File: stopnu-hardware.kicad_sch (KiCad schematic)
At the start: 5 parts, among them CN1 SM04B-SRSS-TB (LF)(SN)

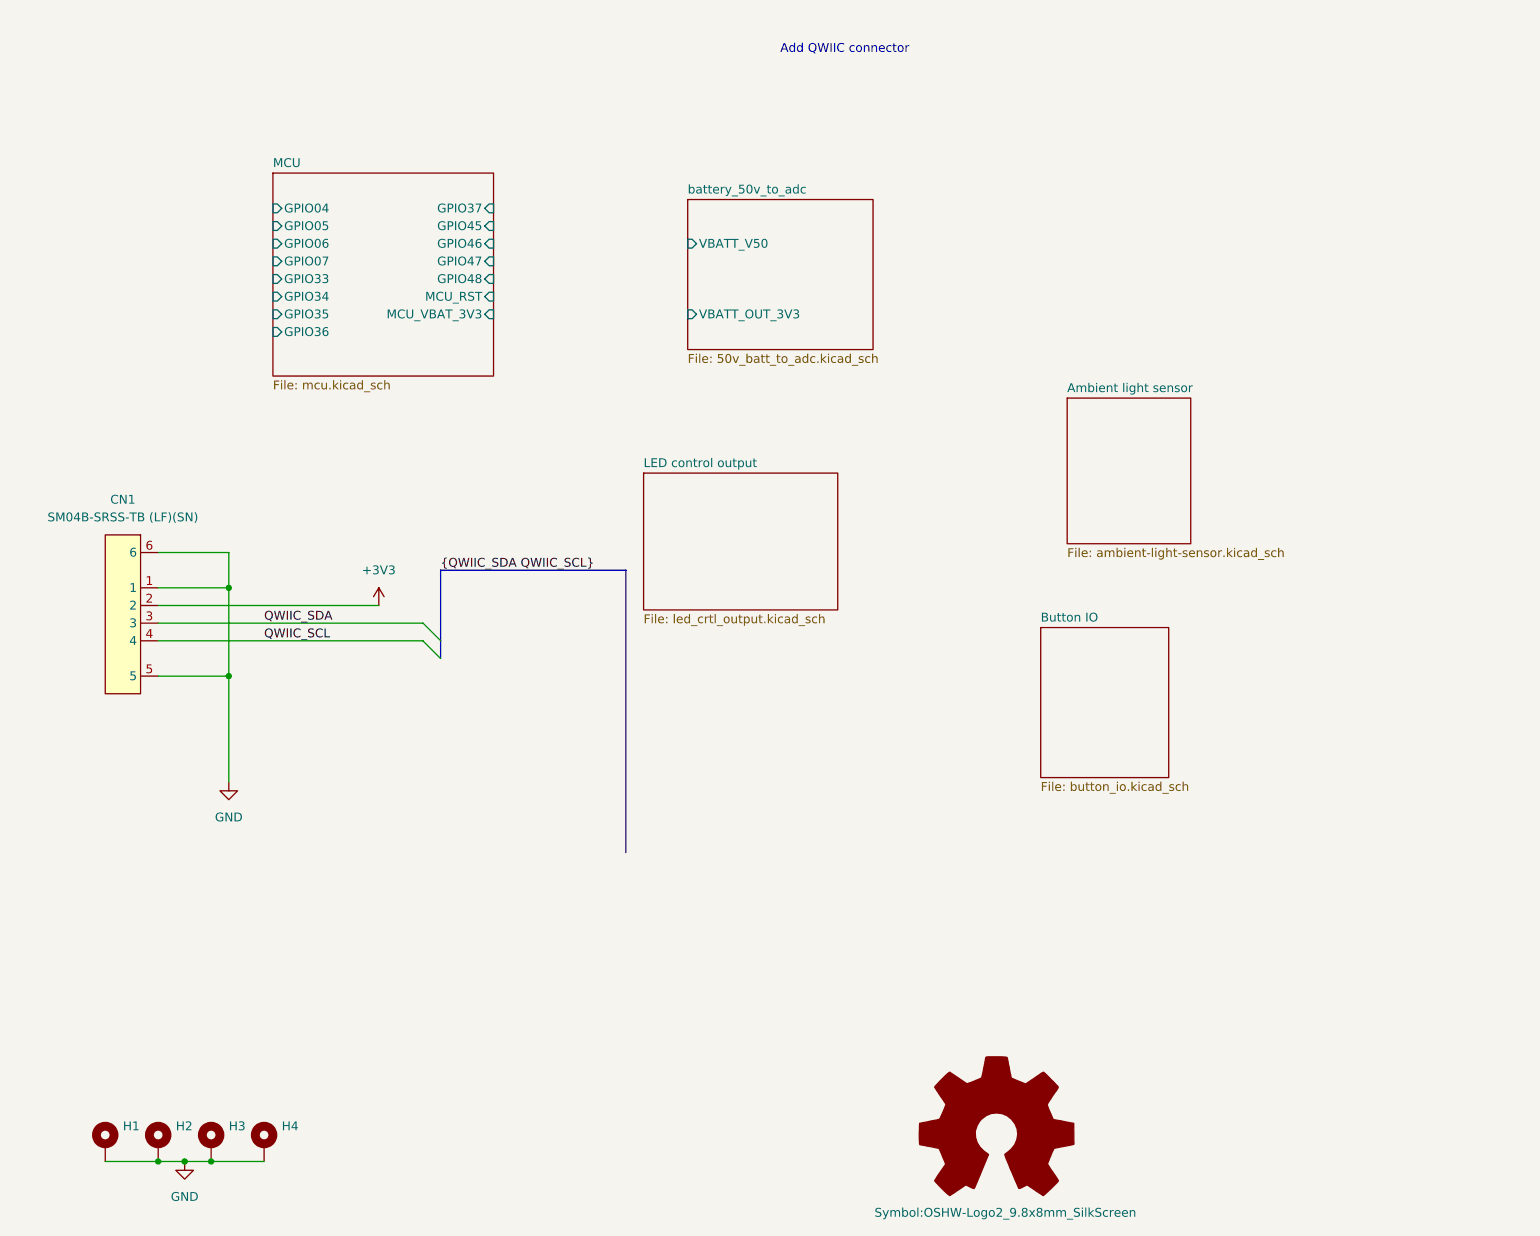
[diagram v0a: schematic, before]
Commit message: Place opto couplers and some connectors.
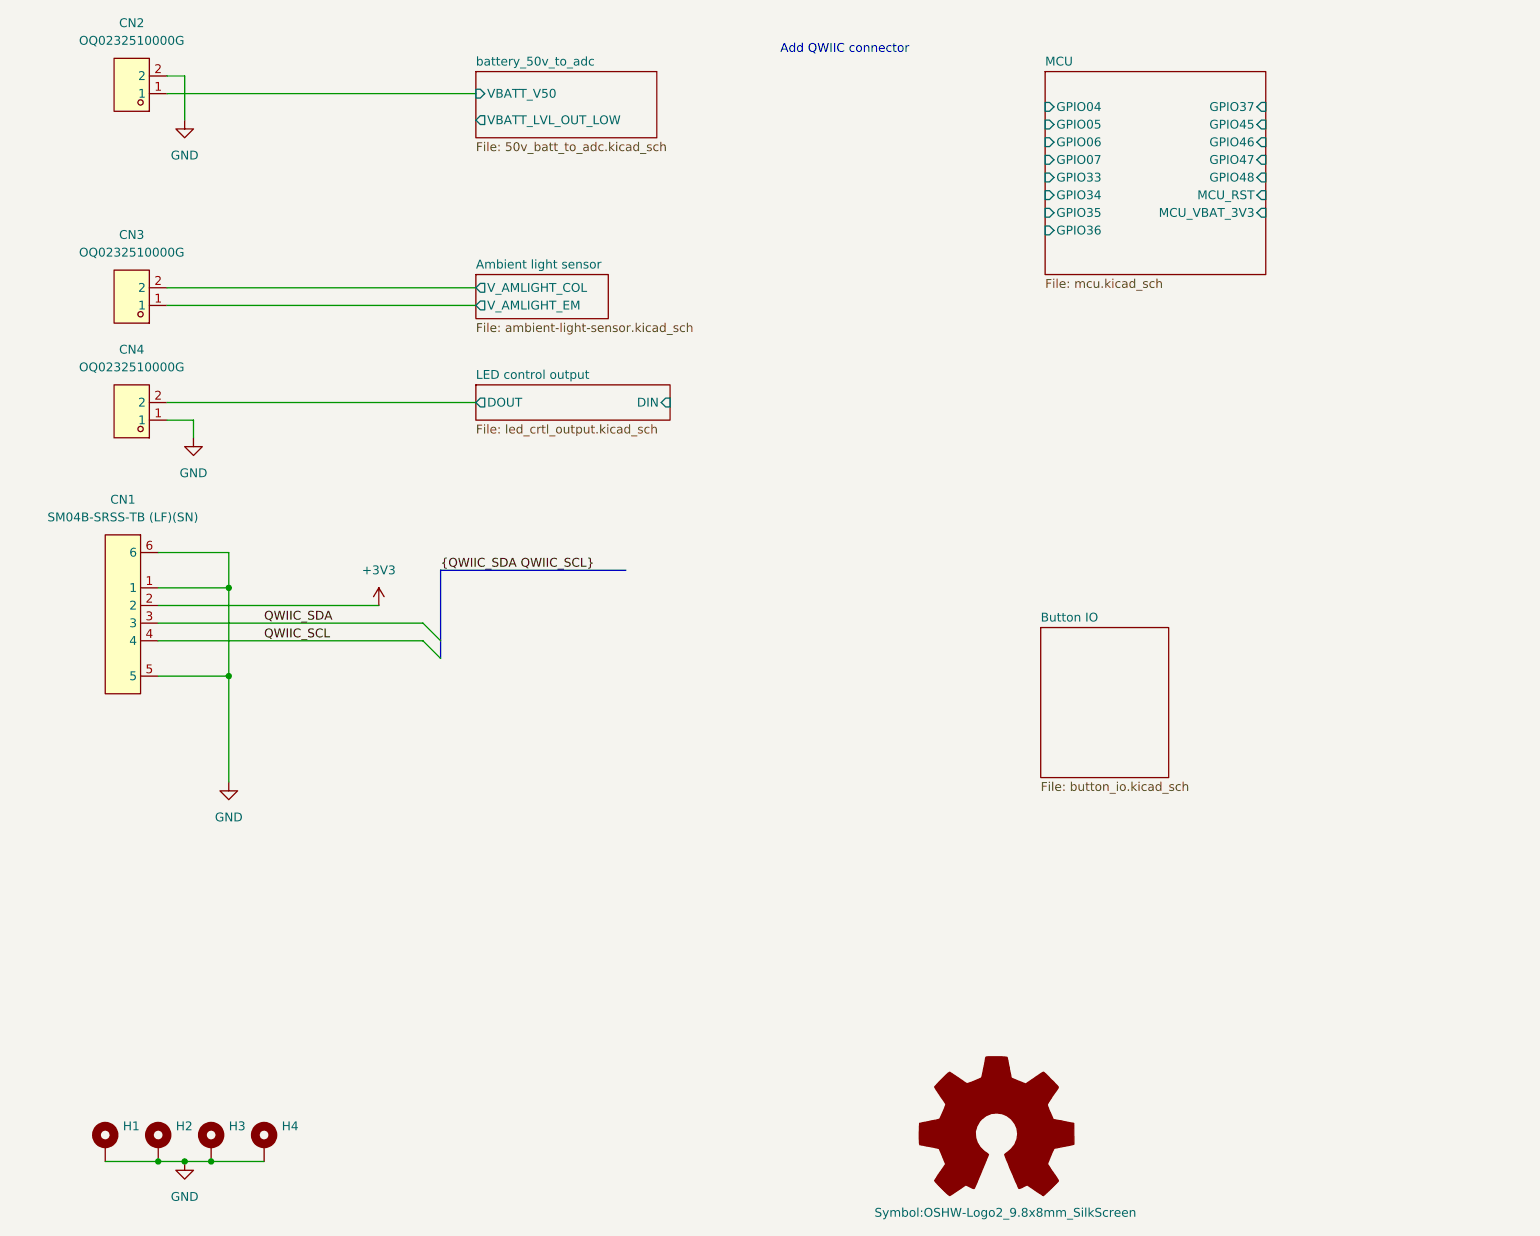
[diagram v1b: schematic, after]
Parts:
- added CN2, CN3, CN4: OQ0232510000G, lcsc:CONN-TH_OQ0232510000G, symbol lcsc:OQ0232510000G
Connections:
- net GND: now also CN2.2, CN4.1
- net battery_50v_to_adc/VBATT_V50: now also CN2.1
- new net Ambient light sensor/V_AMLIGHT_COL: CN3.2
- new net Ambient light sensor/V_AMLIGHT_EM: CN3.1
- new net LED control output/DOUT: CN4.2
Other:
- sheet Ambient light sensor ports: added V_AMLIGHT_COL, V_AMLIGHT_EM; removed none
- sheet LED control output ports: added DIN, DOUT; removed none
- sheet battery_50v_to_adc ports: added VBATT_LVL_OUT_LOW; removed VBATT_OUT_3V3

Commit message: Push schematic stuff missed before.
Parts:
- added CN5: OQ0232510000G, lcsc:CONN-TH_OQ0232510000G, symbol lcsc:OQ0232510000G
- added CN6: OQ0432510000G, lcsc:CONN-TH_4P-P3.81_OQ0432510000G, symbol lcsc:OQ0432510000G
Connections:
- net GND: now also CN6.1
- new net Button IO/BUT_OUT_01: CN6.2
- new net Button IO/BUT_OUT_02: CN6.3
- new net Button IO/BUT_OUT_03: CN6.4
- new net power 5V in/+5V_EXT: CN5.2
- new net power 5V in/GND_EXT: CN5.1
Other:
- added sheet power 5V in (power_5v_in.kicad_sch)
- sheet Button IO ports: added BUT_IN_01, BUT_IN_02, BUT_IN_03, BUT_OUT_01, BUT_OUT_02, BUT_OUT_03; removed none
- sheet MCU ports: added +3V3MCU; removed none
- moved on the sheet: CN1

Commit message: Some extra work for building the rats nest.
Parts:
- removed CN2: OQ0232510000G, lcsc:CONN-TH_OQ0232510000G, symbol lcsc:OQ0232510000G
- added J1: Conn_02x15_Odd_Even, Connector_PinHeader_2.54mm:PinHeader_2x15_P2.54mm_Horizontal, symbol Connector_Generic:Conn_02x15_Odd_Even
- H1, H2, H3, H4: footprint MountingHole:MountingHole_6mm_Pad -> MountingHole:MountingHole_6.4mm_M6_DIN965_Pad
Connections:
- net Button IO/BUT_OUT_01 is gone; now on net Button IO/BUT_IN_03: CN6.2
- net Button IO/BUT_OUT_02 is gone; now on net Button IO/BUT_IN_02: CN6.3
- net Button IO/BUT_OUT_03 is gone; now on net Button IO/BUT_IN_01: CN6.4
- net +3V3: now also J1.16 (Pin_16)
- net GND: now also J1.1 (Pin_1), J1.17 (Pin_17), J1.18 (Pin_18), J1.2 (Pin_2), J1.29 (Pin_29), J1.30 (Pin_30)
- net QWIIC_SCL renamed GPIO48
- net GPIO48: now also J1.22 (Pin_22)
- net QWIIC_SDA renamed GPIO47
- net GPIO47: now also J1.20 (Pin_20)
- new net +5V: J1.15 (Pin_15)
- new net GPIO01: J1.11 (Pin_11)
- new net GPIO02: J1.13 (Pin_13)
- new net GPIO03: J1.19 (Pin_19)
- new net GPIO04: J1.21 (Pin_21)
- new net GPIO05: J1.23 (Pin_23)
- new net GPIO06: J1.25 (Pin_25)
- new net GPIO07: J1.27 (Pin_27)
- new net GPIO26: J1.24 (Pin_24)
- new net GPIO33: J1.14 (Pin_14)
- new net GPIO34: J1.12 (Pin_12)
- new net GPIO38: J1.9 (Pin_9)
- new net GPIO39: J1.7 (Pin_7)
- new net GPIO40: J1.5 (Pin_5)
- new net GPIO41: J1.3 (Pin_3)
- new net MCU_RST: J1.8 (Pin_8)
- new net UART_RX: J1.6 (Pin_6)
- new net UART_TX: J1.4 (Pin_4)
- new net USER_KEY: J1.10 (Pin_10)
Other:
- sheet MCU renamed HELTEC V3
- removed sheet battery_50v_to_adc
- sheet HELTEC V3 ports: added GPIO01, GPIO02, GPIO03, GPIO26, GPIO38, GPIO39, GPIO40, GPIO41, GPIO42, OLED_RST, UART_RX, UART_TX, USB_D+, USB_D-, USER_KEY; removed GPIO35, GPIO36, GPIO37, GPIO45, GPIO46

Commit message: WIP: Routed version, for first feedback round
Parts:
- added CN2: OQ0232510000G, lcsc:CONN-TH_OQ0232510000G, symbol lcsc:OQ0232510000G
- added D1: D5V0P4URL6SO-7, lcsc:SOT-26_L3.0-W1.6-P0.95-LS2.8-BL, symbol lcsc:D5V0P4URL6SO-7
- added N1: Viking Art, footprints:StopNuVikings, symbol Mechanical:Housing
- added R1, R2: 2k, Resistor_SMD:R_0603_1608Metric, symbol Device:R_Small
- CN4: Label2 (none) -> LED1
- CN5: Label2 (none) -> Power 5V
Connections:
- net Ambient light sensor/V_AMLIGHT_EM is gone; now on net GPIO02: CN3.1
- net +3V3: now also J1.15 (Pin_15), R1.1, R2.1; no longer J1.16 (Pin_16)
- net +5V: now also J1.16 (Pin_16); no longer J1.15 (Pin_15)
- net GND: now also CN2.1, D1.2 (VSS)
- net GPIO47: now also D1.1 (I/O1), D1.6 (I/O4), R1.2
- net GPIO48: now also D1.3 (I/O2), D1.4 (I/O3), R2.2
- new net LED control output 2/DOUT: CN2.2
- no-connect marks 0 -> 1
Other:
- sheet LED control output renamed LED control output 1
- added sheet LED control output 2 (led_crtl_output.kicad_sch)
- sheet HELTEC V3 ports: added +3V3_MCU; removed +3V3MCU
- sheet power 5V in ports: added +3V3_MCU; removed +3V3MCU
- moved on the sheet: CN6

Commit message: minor improvements.
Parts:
- added N2: Open Hardware, Symbol:OSHW-Logo2_9.8x8mm_SilkScreen, symbol Mechanical:Housing
- added N3: Ranzlogo, footprints:goatse_01, symbol Mechanical:Housing
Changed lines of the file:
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@@
+	)
+	(symbol
+		(lib_id "Mechanical:Housing")
+		(at 121.92 180.34 0)
+		(unit 1)
+		(exclude_from_sim no)
+		(in_bom yes)
+		(on_board yes)
+		(dnp no)
+		(fields_autoplaced yes)
+		(property "Reference" "N3"
+			(at 125.73 179.3874 0)
+			(effects
+				(font
+					(size 1.27 1.27)
+				)
+				(justify left)
+			)
+		)
+		(property "Value" "Ranzlogo"
+			(at 125.73 181.9274 0)
+			(effects
+				(font
+					(size 1.27 1.27)
+				)
+				(justify left)
+			)
+		)
+		(property "Footprint" "footprints:goatse_01"
+			(at 123.19 179.07 0)
+			(effects
+				(font
+					(size 1.27 1.27)
+				)
+				(hide yes)
+			)
+		)
+		(property "Datasheet" "~"
+			(at 123.19 179.07 0)
+			(effects
+				(font
+					(size 1.27 1.27)
+				)
+				(hide yes)
+			)
+		)
+		(property "Description" "Housing"
+			(at 121.92 180.34 0)
+			(effects
+				(font
+					(size 1.27 1.27)
+				)
+				(hide yes)
+			)
+		)
+		(instances
+			(project "stopnu-hardware"
+				(path "/4ab90003-ea4c-4878-8117-f834ac24f8d9"
+					(reference "N3")
+					(unit 1)
+				)
+			)
+		)
+	)
+	(symbol
+		(lib_id "Mechanical:Housing")
+		(at 96.52 181.61 0)
+		(unit 1)
+		(exclude_from_sim no)
+		(in_bom yes)
+		(on_board yes)
+		(dnp no)
+		(fields_autoplaced yes)
+		(property "Reference" "N2"
+			(at 100.33 180.6574 0)
+			(effects
+				(font
+					(size 1.27 1.27)
+				)
+				(justify left)
+			)
+		)
+		(property "Value" "Open Hardware"
+			(at 100.33 183.1974 0)
+			(effects
+				(font
+					(size 1.27 1.27)
+				)
+				(justify left)
+			)
+		)
+		(property "Footprint" "Symbol:OSHW-Logo2_9.8x8mm_SilkScreen"
+			(at 97.79 180.34 0)
+			(effects
+				(font
+					(size 1.27 1.27)
+				)
+				(hide yes)
+			)
+		)
+		(property "Datasheet" "~"
+			(at 97.79 180.34 0)
+			(effects
+				(font
+					(size 1.27 1.27)
+				)
+				(hide yes)
+			)
+		)
+		(property "Description" "Housing"
+			(at 96.52 181.61 0)
+			(effects
+				(font
+					(size 1.27 1.27)
+				)
+				(hide yes)
+			)
+		)
+		(instances
+			(project "stopnu-hardware"
+				(path "/4ab90003-ea4c-4878-8117-f834ac24f8d9"
+					(reference "N2")
+					(unit 1)
+				)
+			)
+		)
 	)
 	(symbol

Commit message: Mounting holes to 4.5mm.
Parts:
- H1, H2, H3, H4: footprint MountingHole:MountingHole_6.4mm_M6_DIN965_Pad -> MountingHole:MountingHole_4.5mm_Pad_Via
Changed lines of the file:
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@@
 			)
 		)
-		(property "Footprint" "MountingHole:MountingHole_6.4mm_M6_DIN965_Pad"
+		(property "Footprint" "MountingHole:MountingHole_4.5mm_Pad_Via"
 			(at 39.37 177.8 0)
 			(effects
@@
 			)
 		)
-		(property "Footprint" "MountingHole:MountingHole_6.4mm_M6_DIN965_Pad"
+		(property "Footprint" "MountingHole:MountingHole_4.5mm_Pad_Via"
 			(at 46.99 177.8 0)
 			(effects
@@
 			)
 		)
-		(property "Footprint" "MountingHole:MountingHole_6.4mm_M6_DIN965_Pad"
+		(property "Footprint" "MountingHole:MountingHole_4.5mm_Pad_Via"
 			(at 31.75 177.8 0)
 			(effects
@@
 			)
 		)
-		(property "Footprint" "MountingHole:MountingHole_6.4mm_M6_DIN965_Pad"
+		(property "Footprint" "MountingHole:MountingHole_4.5mm_Pad_Via"
 			(at 24.13 177.8 0)
 			(effects

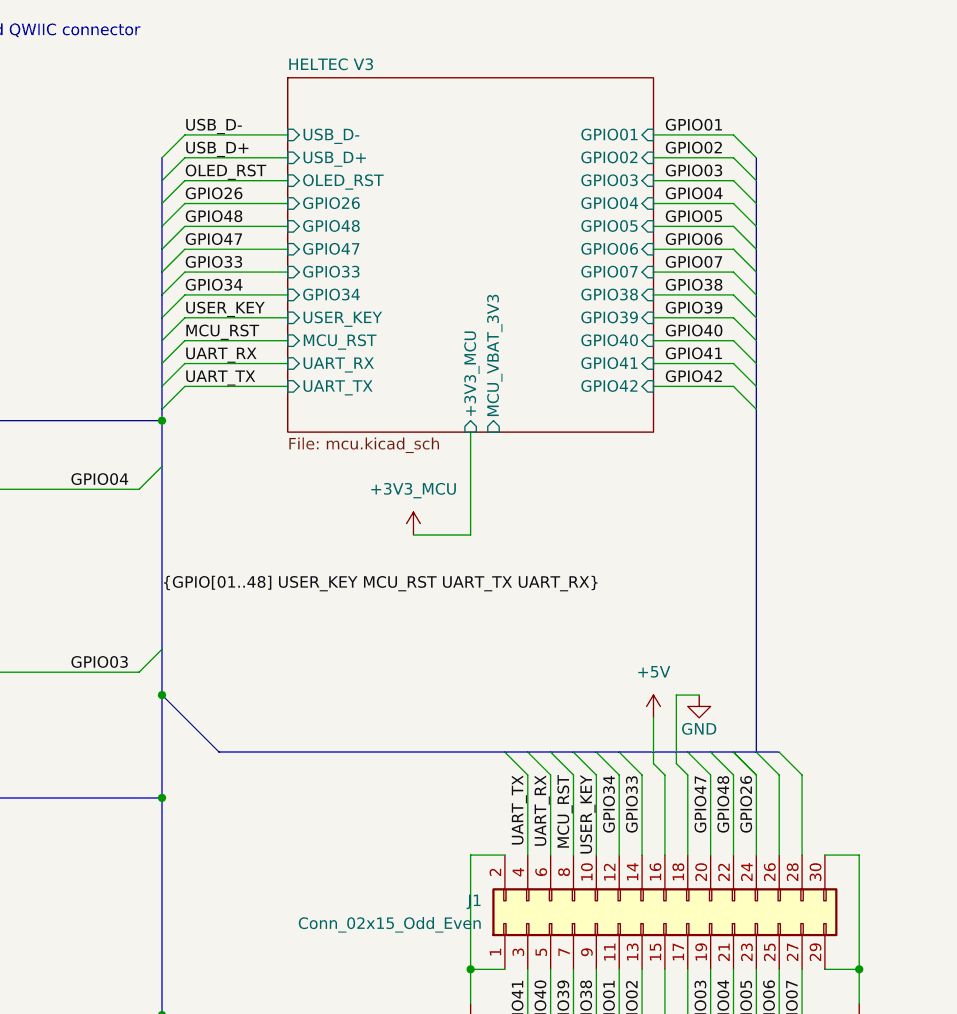
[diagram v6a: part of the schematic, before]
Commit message: Fixed USB-pin routing, some other cleanups.
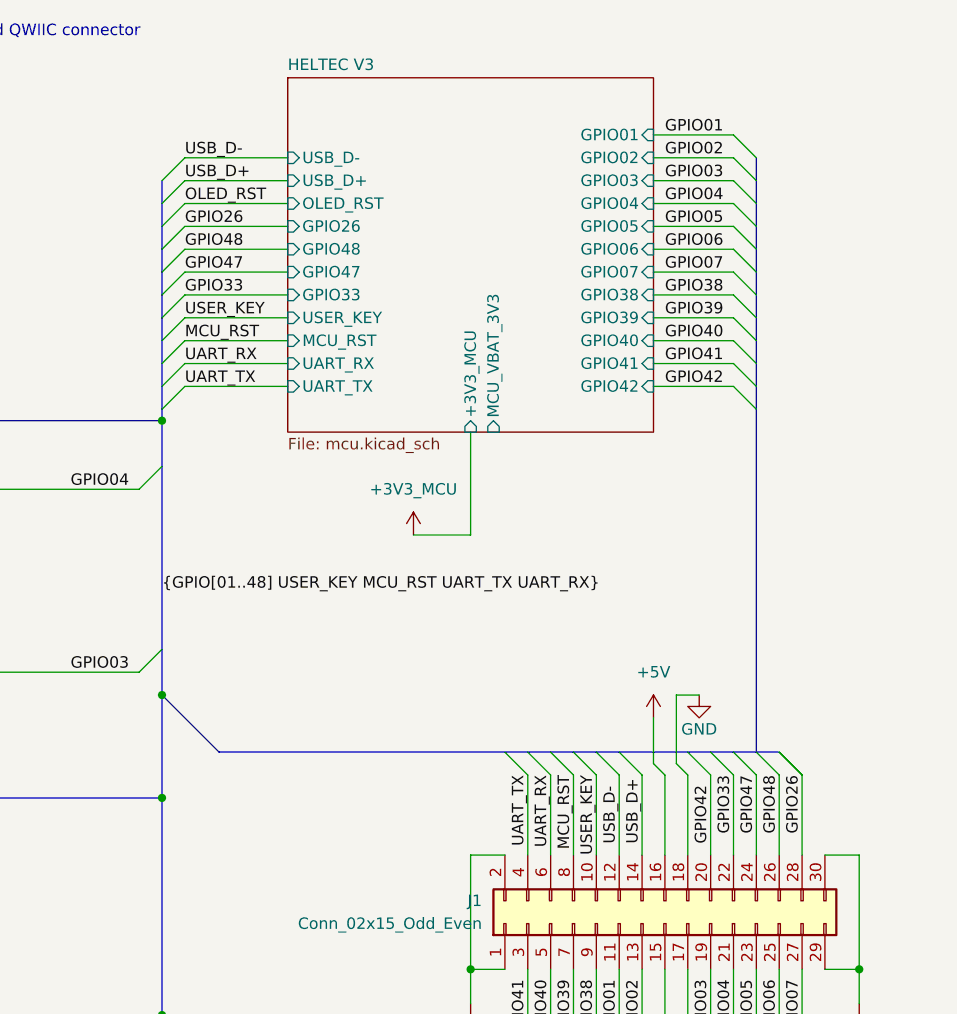
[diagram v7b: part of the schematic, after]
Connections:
- net GPIO34 is gone; now on net USB_D-: J1.12 (Pin_12)
- net GPIO26: now also J1.28 (Pin_28); no longer J1.24 (Pin_24)
- net GPIO33: now also J1.22 (Pin_22); no longer J1.14 (Pin_14)
- net GPIO42: now also J1.20 (Pin_20)
- net GPIO47: now also J1.24 (Pin_24); no longer J1.20 (Pin_20)
- net GPIO48: now also J1.26 (Pin_26); no longer J1.22 (Pin_22)
- net USB_D+: now also J1.14 (Pin_14)
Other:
- sheet HELTEC V3 ports: added none; removed GPIO34

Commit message: Labeled expansion port, fixed en pin U19 (high)
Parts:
- CN2, CN4: GND (none) -> GND; S (none) -> S
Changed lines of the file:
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@@
+			)
+		)
+		(property "GND" "GND"
+			(at 27.94 72.39 0)
+			(effects
+				(font
+					(size 1.27 1.27)
+				)
+				(hide yes)
+			)
+		)
+		(property "S" "S"
+			(at 27.94 72.39 0)
+			(effects
+				(font
+					(size 1.27 1.27)
+				)
+				(hide yes)
 			)
 		)
@@
 			)
 		)
+		(property "GND" "GND"
+			(at 27.94 92.71 0)
+			(effects
+				(font
+					(size 1.27 1.27)
+				)
+				(hide yes)
+			)
+		)
+		(property "S" "S"
+			(at 27.94 92.71 0)
+			(effects
+				(font
+					(size 1.27 1.27)
+				)
+				(hide yes)
+			)
+		)
